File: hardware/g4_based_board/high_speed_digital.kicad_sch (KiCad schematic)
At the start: 22 parts, among them J10 DE9_Receptacle, J11 DE9_Receptacle, J12 DE9_Receptacle, J13 DE9_Receptacle, J14 DE9_Receptacle, J15 DE9_Receptacle, J16 DE9_Receptacle, J17 DE9_Receptacle, J18 DE9_Receptacle, J3 DE9_Receptacle, J4 DE9_Receptacle, J5 DE9_Receptacle, J6 DE9_Receptacle, J7 DE9_Receptacle, J8 DE9_Receptacle, J9 DE9_Receptacle, U3 74HC4024

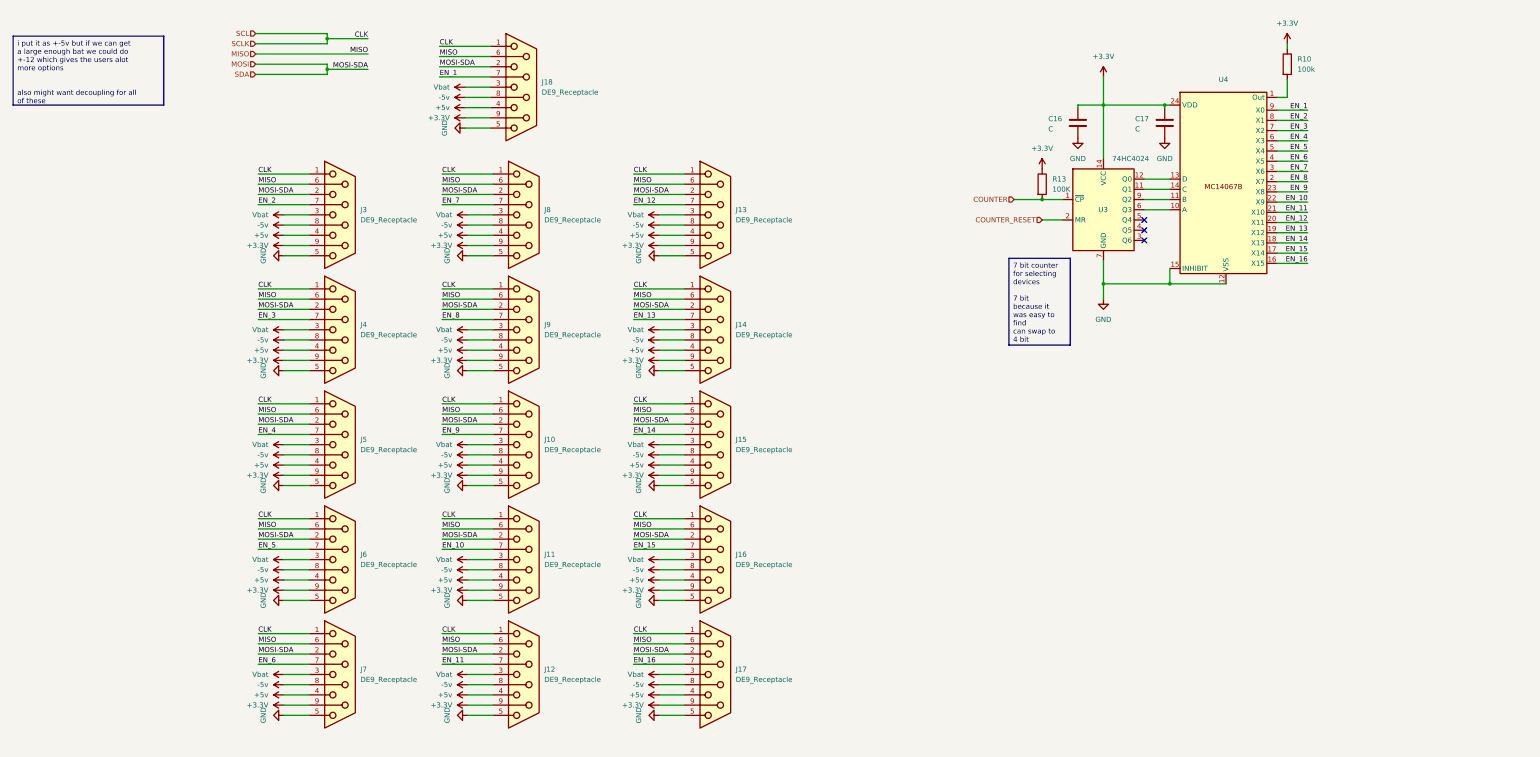
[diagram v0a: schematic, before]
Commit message: removed 8 ports as it was too many
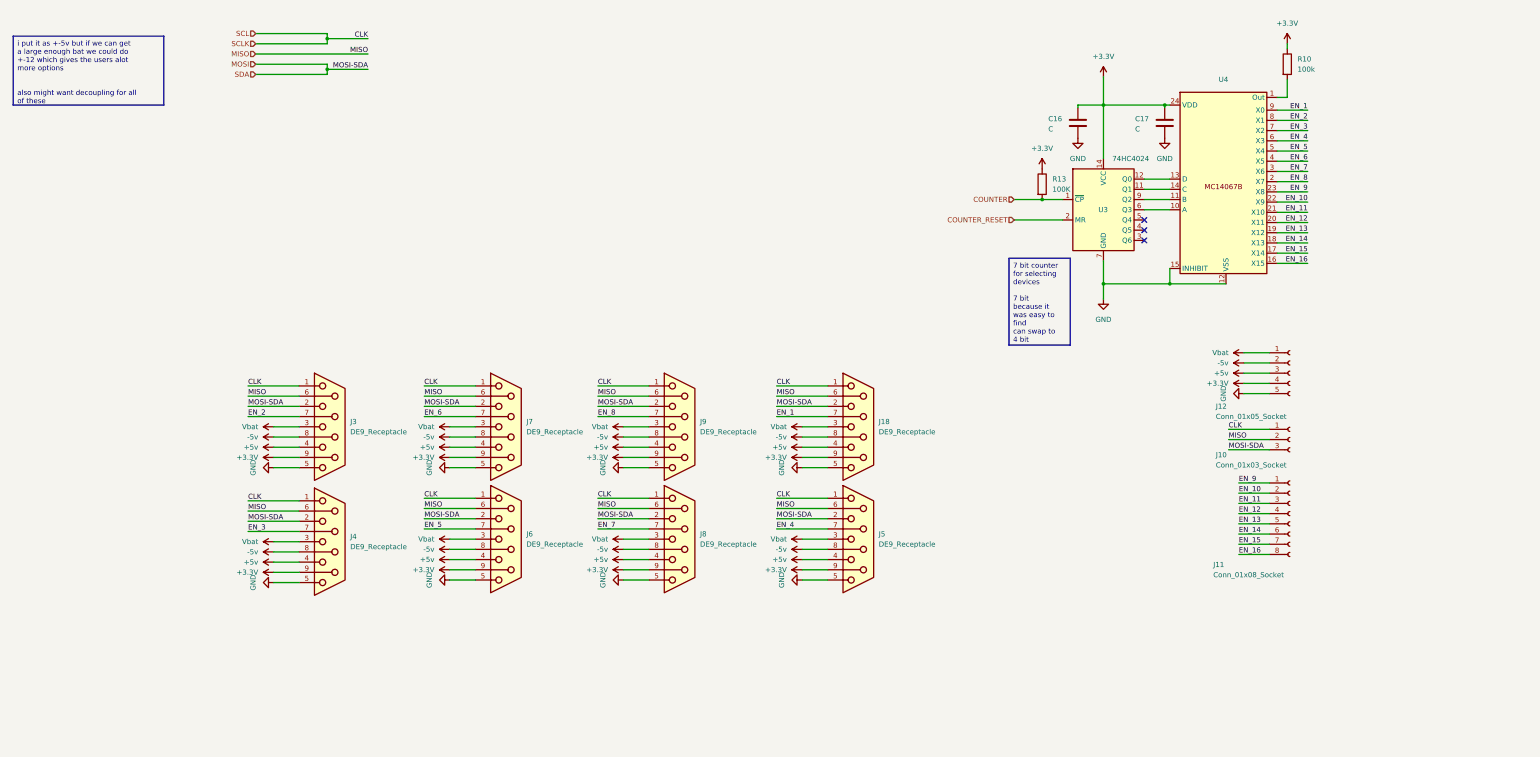
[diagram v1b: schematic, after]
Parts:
- removed J10, J11, J12, J13, J14, J15, J16, J17: DE9_Receptacle, Connector_Dsub:DSUB-9_Female_Vertical_P2.77x2.84mm_MountingHoles, symbol Connector:DE9_Receptacle
- added J10: Conn_01x03_Socket, symbol Connector:Conn_01x03_Socket
- added J11: Conn_01x08_Socket, symbol Connector:Conn_01x08_Socket
- added J12: Conn_01x05_Socket, symbol Connector:Conn_01x05_Socket
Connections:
- net +3.3V: now also J12.4 (Pin_4)
- net +5v: now also J12.3 (Pin_3)
- net -5v: now also J12.2 (Pin_2)
- net EN_10: now also J11.2 (Pin_2)
- net EN_11: now also J11.3 (Pin_3)
- net EN_12: now also J11.4 (Pin_4)
- net EN_13: now also J11.5 (Pin_5)
- net EN_14: now also J11.6 (Pin_6)
- net EN_15: now also J11.7 (Pin_7)
- net EN_16: now also J11.8 (Pin_8)
- net EN_9: now also J11.1 (Pin_1)
- net GND: now also J12.5 (Pin_5)
- net MISO: now also J10.2 (Pin_2)
- net MOSI: now also J10.3 (Pin_3)
- net SCL: now also J10.1 (Pin_1)
- net Vbat: now also J12.1 (Pin_1)
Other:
- moved on the sheet: J18, J3, J4, J5, J6, J7, J8, J9

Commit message: removed half of the digial interfaces and added the thermocouples and LCD modules in to this sheet
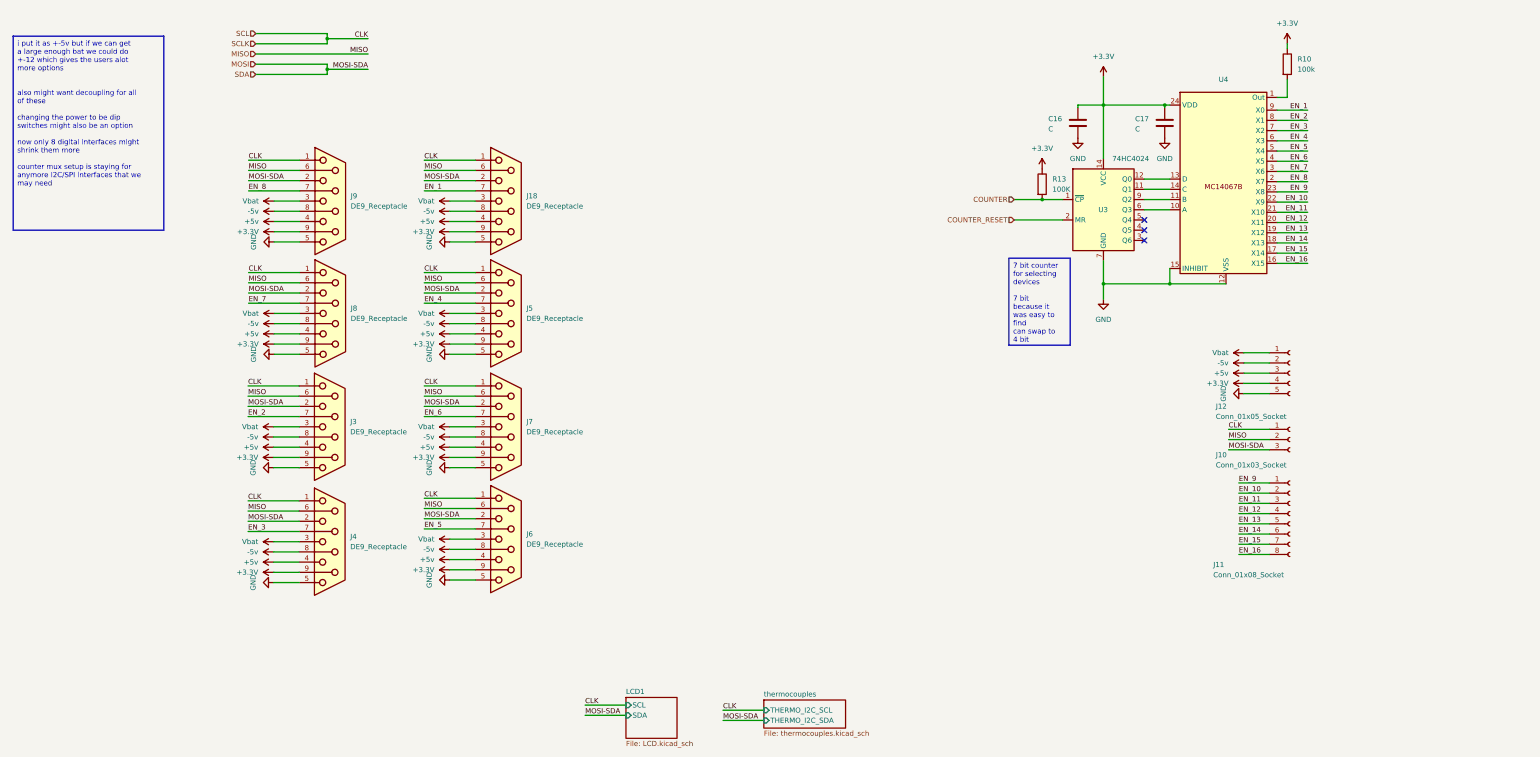
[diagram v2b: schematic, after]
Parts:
- R13: footprint (none) -> Resistor_SMD:R_0805_2012Metric
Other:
- added sheet LCD1 (LCD.kicad_sch)
- added sheet thermocouples (thermocouples.kicad_sch)
- moved on the sheet: J18, J5, J8, J9

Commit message: changed to having seprate I2C and SPI lines with switches for power select
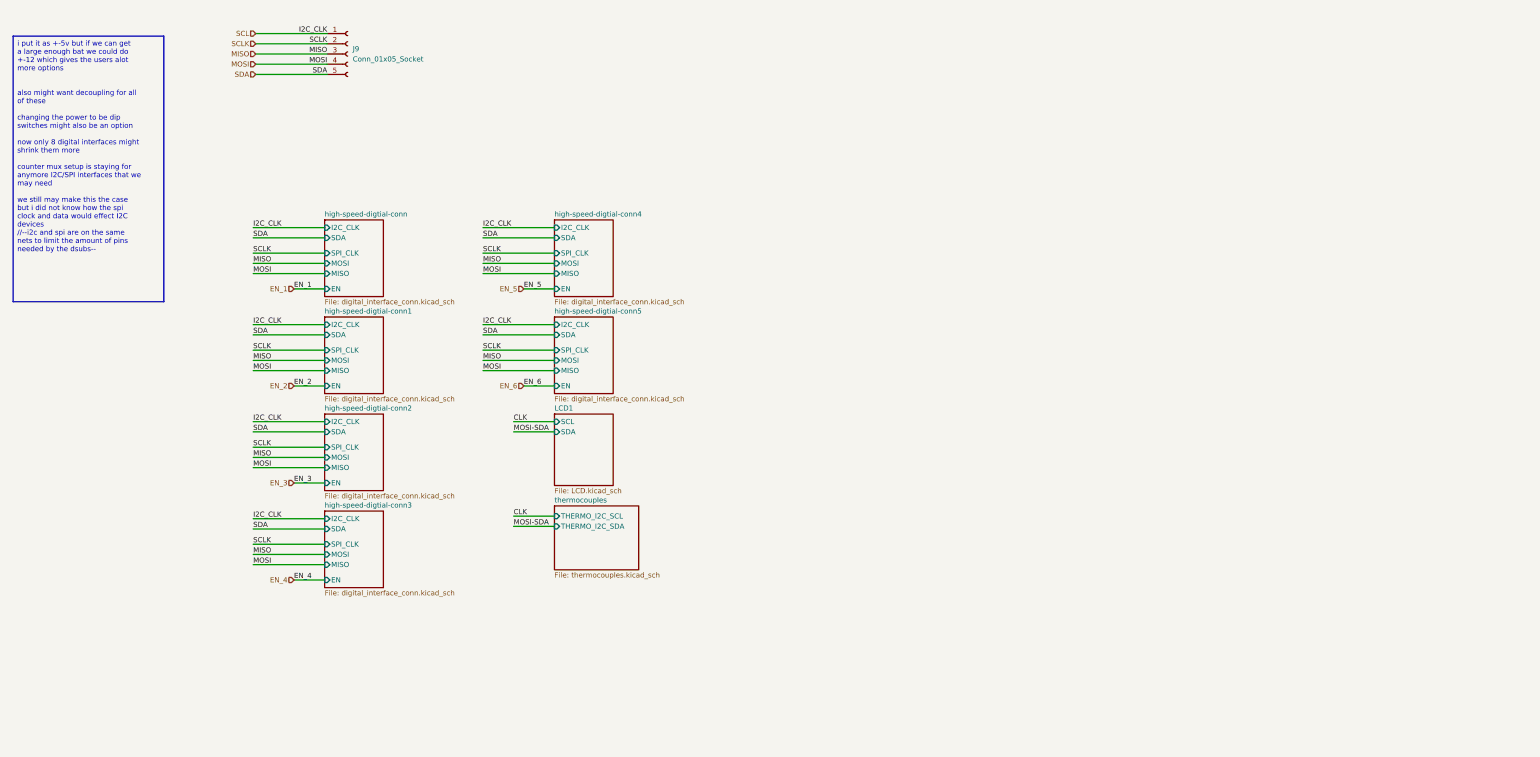
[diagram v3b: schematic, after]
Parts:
- removed C16, C17: C, Capacitor_SMD:C_0805_2012Metric, symbol Device:C
- removed J10: Conn_01x03_Socket, symbol Connector:Conn_01x03_Socket
- removed J11: Conn_01x08_Socket, symbol Connector:Conn_01x08_Socket
- removed J12: Conn_01x05_Socket, symbol Connector:Conn_01x05_Socket
- removed J18, J3, J4, J5, J6, J7, J8, J9: DE9_Receptacle, Connector_Dsub:DSUB-9_Female_Vertical_P2.77x2.84mm_MountingHoles, symbol Connector:DE9_Receptacle
- removed R10: 100k, Resistor_SMD:R_0805_2012Metric, symbol Device:R
- removed R13: 100K, Resistor_SMD:R_0805_2012Metric, symbol Device:R
- removed U3: 74HC4024, Package_SO:SOIC-14_3.9x8.7mm_P1.27mm, symbol 74xx:74HC4024
- removed U4: ~, Package_SO:SOIC-24W_7.5x15.4mm_P1.27mm, symbol parts_not_in_kicad:MC14067B
- added J9: Conn_01x05_Socket, Connector_PinHeader_2.54mm:PinHeader_1x05_P2.54mm_Vertical, symbol Connector:Conn_01x05_Socket
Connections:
- net MISO: now also J9.3 (Pin_3)
- net MOSI: now also J9.4 (Pin_4)
- net SCL: now also J9.1 (Pin_1)
- new net SCLK: J9.2 (Pin_2)
- new net SDA: J9.5 (Pin_5)
- no-connect marks 3 -> 0
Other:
- added sheet high-speed-digtial-conn (digital_interface_conn.kicad_sch)
- added sheet high-speed-digtial-conn1 (digital_interface_conn.kicad_sch)
- added sheet high-speed-digtial-conn2 (digital_interface_conn.kicad_sch)
- added sheet high-speed-digtial-conn3 (digital_interface_conn.kicad_sch)
- added sheet high-speed-digtial-conn4 (digital_interface_conn.kicad_sch)
- added sheet high-speed-digtial-conn5 (digital_interface_conn.kicad_sch)

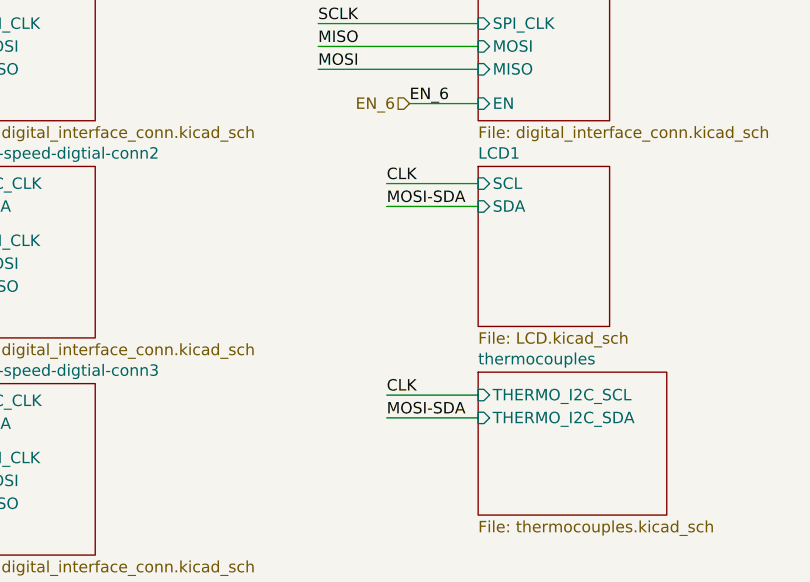
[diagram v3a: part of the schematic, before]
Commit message: removed spi expander and now uses mcu pins for enable
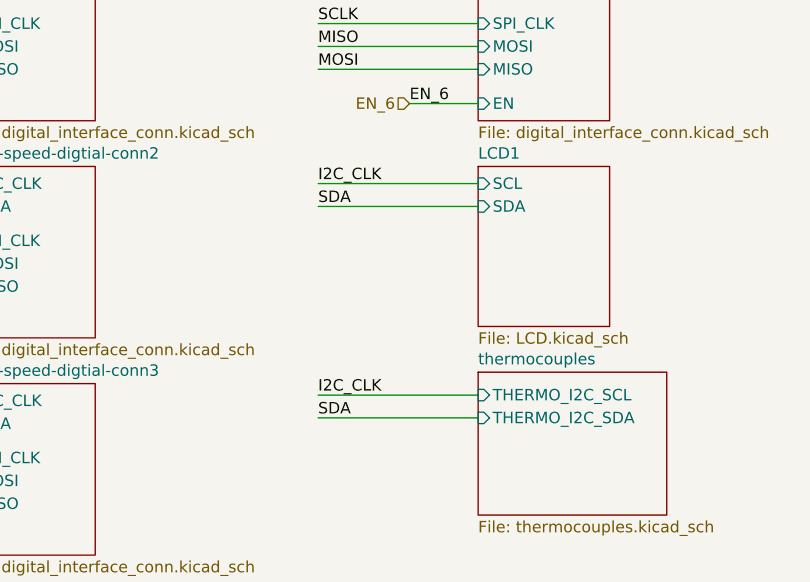
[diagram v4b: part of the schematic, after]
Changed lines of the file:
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@@
+	(wire
+		(pts
+			(xy 94.615 141.605) (xy 76.835 141.605)
+		)
+		(stroke
+			(width 0)
+			(type default)
+		)
+	)
 	(wire
 		(pts
@@
 	(wire
 		(pts
+			(xy 94.615 115.57) (xy 76.835 115.57)
+		)
+		(stroke
+			(width 0)
+			(type default)
+		)
+	)
+	(wire
+		(pts
 			(xy 94.615 73.66) (xy 76.835 73.66)
 		)
@@
 	(wire
 		(pts
-			(xy 94.615 141.605) (xy 84.455 141.605)
-		)
-		(stroke
-			(width 0)
-			(type default)
-		)
-	)
-	(wire
-		(pts
 			(xy 37.465 148.59) (xy 19.685 148.59)
 		)
@@
 	(wire
 		(pts
+			(xy 94.615 139.065) (xy 76.835 139.065)
+		)
+		(stroke
+			(width 0)
+			(type default)
+		)
+	)
+	(wire
+		(pts
 			(xy 37.465 130.81) (xy 29.845 130.81)
 		)
@@
 	(wire
 		(pts
-			(xy 94.615 139.065) (xy 84.455 139.065)
-		)
-		(stroke
-			(width 0)
-			(type default)
-		)
-	)
-	(wire
-		(pts
-			(xy 94.615 115.57) (xy 84.455 115.57)
-		)
-		(stroke
-			(width 0)
-			(type default)
-		)
-	)
-	(wire
-		(pts
 			(xy 37.465 121.92) (xy 19.685 121.92)
 		)
@@
 	(wire
 		(pts
+			(xy 94.615 118.11) (xy 76.835 118.11)
+		)
+		(stroke
+			(width 0)
+			(type default)
+		)
+	)
+	(wire
+		(pts
 			(xy 37.465 93.98) (xy 19.685 93.98)
 		)
@@
 		(pts
 			(xy 94.615 93.98) (xy 76.835 93.98)
-		)
-		(stroke
-			(width 0)
-			(type default)
-		)
-	)
-	(wire
-		(pts
-			(xy 94.615 118.11) (xy 84.455 118.11)
 		)
 		(stroke
@@
 		)
 	)
-	(label "MOSI-SDA"
-		(at 84.455 118.11 0)
-		(fields_autoplaced yes)
-		(effects
-			(font
-				(size 1.27 1.27)
-			)
-			(justify left bottom)
-		)
-	)
-	(label "CLK"
-		(at 84.455 115.57 0)
-		(fields_autoplaced yes)
-		(effects
-			(font
-				(size 1.27 1.27)
-			)
-			(justify left bottom)
-		)
-	)
 	(label "I2C_CLK"
 		(at 19.685 139.7 0)
-		(fields_autoplaced yes)
-		(effects
-			(font
-				(size 1.27 1.27)
-			)
-			(justify left bottom)
-		)
-	)
-	(label "MOSI-SDA"
-		(at 84.455 141.605 0)
 		(fields_autoplaced yes)
 		(effects
@@
 		)
 	)
+	(label "I2C_CLK"
+		(at 76.835 115.57 0)
+		(fields_autoplaced yes)
+		(effects
+			(font
+				(size 1.27 1.27)
+			)
+			(justify left bottom)
+		)
+	)
 	(label "SDA"
 		(at 19.685 93.98 0)
@@
 		)
 	)
-	(label "CLK"
-		(at 84.455 139.065 0)
+	(label "I2C_CLK"
+		(at 76.835 139.065 0)
 		(fields_autoplaced yes)
 		(effects
@@
 		(fields_autoplaced yes)
 		(effects
+			(font
+				(size 1.27 1.27)
+			)
+			(justify left bottom)
+		)
+	)
+	(label "SDA"
+		(at 76.835 118.11 0)
+		(fields_autoplaced yes)
+		(effects
+			(font
+				(size 1.27 1.27)
+			)
+			(justify left bottom)
+		)
+	)
+	(label "SDA"
+		(at 76.835 141.605 0)
+		(fields_autoplaced yes)
+		(effects
